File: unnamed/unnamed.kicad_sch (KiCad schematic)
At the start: 126 parts, among them J1 Serial, J2 Serial, J3 Conn_01x01_Female, J4 Conn_01x01_Female, J5 S3B-PH-SM4-TB(LF)(SN), J6 S3B-PH-SM4-TB(LF)(SN), J7 Conn_01x12_Female, J8 Conn_01x12_Female, SW1 SW_Push, SW10 SW_Push, SW11 SW_Push, SW12 SW_Push, SW13 SW_Push, SW14 SW_Push, SW15 SW_Push, SW16 SW_Push, SW17 SW_Push, SW18 SW_Push, SW19 SW_Push, SW2 SW_Push, SW20 SW_Push, SW21 SW_Push, SW22 SW_Push, SW23 SW_Push, SW24 SW_Push, SW25 SW_SPST, SW26 SW_SPST, SW27 SW_Push, SW28 SW_Push, SW29 SW_Push, SW3 SW_Push, SW30 SW_Push, SW31 SW_Push, SW32 SW_Push, SW33 SW_Push, SW34 SW_Push, SW35 SW_Push, SW36 SW_Push, SW4 SW_Push, SW5 SW_Push, SW6 SW_Push, SW7 SW_Push, SW8 SW_Push, SW9 SW_Push, U1 eliteC, U2 eliteC

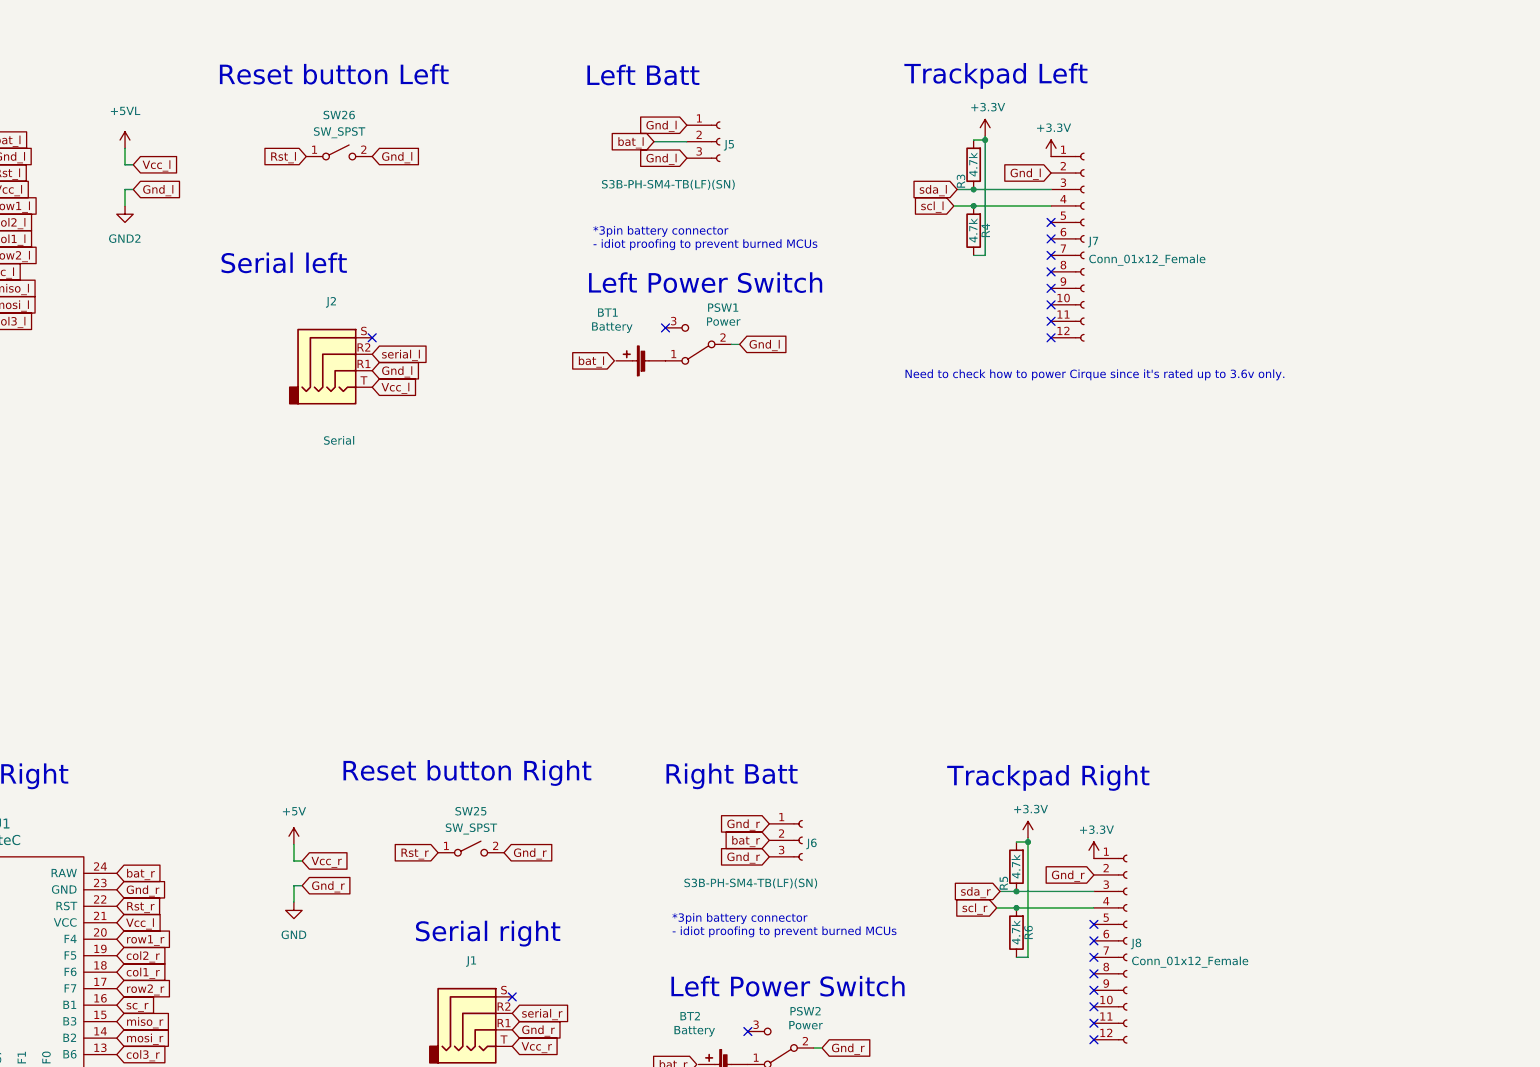
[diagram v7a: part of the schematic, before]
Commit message: Added OLED
SSD1306 OLED. Might include jumpers to bigger SH1107 (hi drashna!) OLED. Also planning to ad SPI screen pin headers.
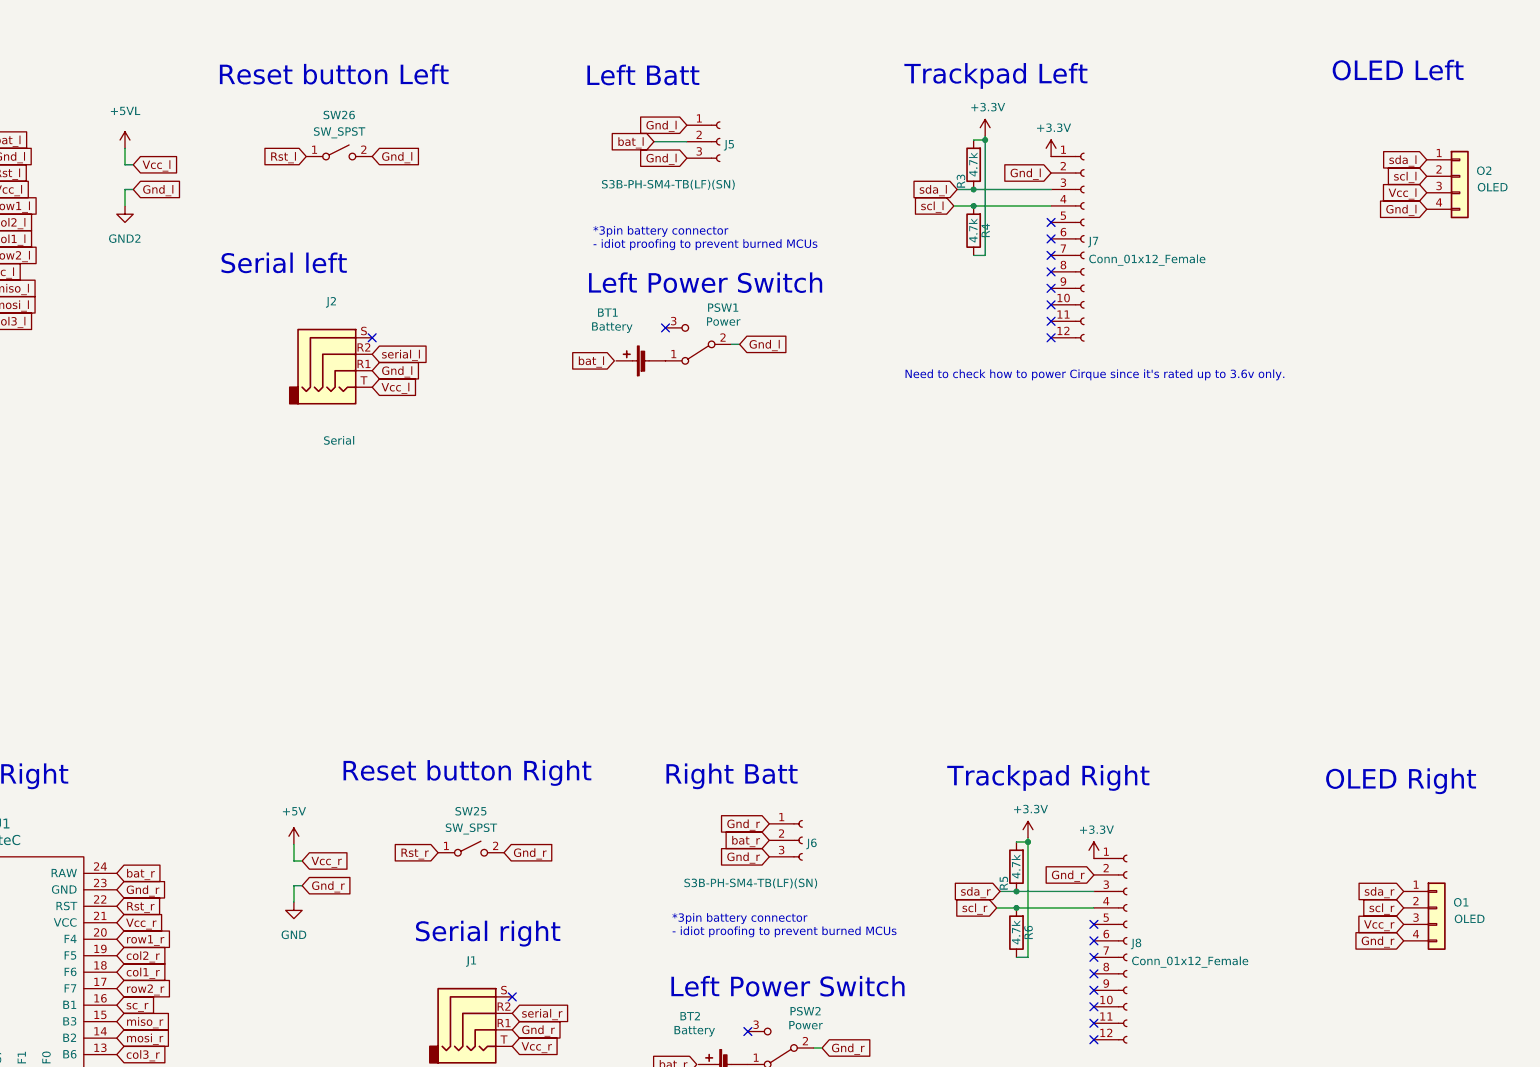
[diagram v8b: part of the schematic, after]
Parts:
- added O1, O2: OLED, swoop:OLED_jumpers, symbol Connector_Generic:Conn_01x04
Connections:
- net +5V: now also U1.21 (VCC), O1.3 (Pin_3)
- net +5VL: now also O2.3 (Pin_3); no longer U1.21 (VCC)
- net GND: now also O1.4 (Pin_4)
- net GND2: now also O2.4 (Pin_4)
- net scl_l: now also O2.2 (Pin_2)
- net scl_r: now also O1.2 (Pin_2)
- net sda_l: now also O2.1 (Pin_1)
- net sda_r: now also O1.1 (Pin_1)
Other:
- note added: "OLED Left"
- note added: "OLED Right"
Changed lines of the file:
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@@
     (effects (font (size 3 3)) (justify left bottom))
   )
+  (text "OLED Right" (at 525.272 136.144 0)
+    (effects (font (size 3 3)) (justify left bottom))
+  )
   (text "Reset button Right" (at 373.634 134.874 0)
     (effects (font (size 3 3)) (justify left bottom))
@@
     (effects (font (size 5 5)) (justify left bottom))
   )
+  (text "OLED Left" (at 526.288 26.924 0)
+    (effects (font (size 3 3)) (justify left bottom))
+  )
   (text "RGB - plate and thumb cluster" (at 73.3044 168.2242 180)
     (effects (font (size 1.27 1.27)) (justify right bottom))
@@
     )
   )
+  (global_label "sda_r" (shape input) (at 537.464 151.384 180)
+    (effects (font (size 1.27 1.27)) (justify right))
+    (property "Intersheet References" "${INTERSHEET_REFS}" (id 0) (at 508.254 96.774 0)
+      (effects (font (size 1.27 1.27)) hide)
+    )
+  )
   (global_label "Gnd_l" (shape input) (at 303.53 156.21 180)
     (effects (font (size 1.27 1.27)) (justify right))
@@
     )
   )
+  (global_label "scl_r" (shape input) (at 537.464 153.924 180)
+    (effects (font (size 1.27 1.27)) (justify right))
+    (property "Intersheet References" "${INTERSHEET_REFS}" (id 0) (at 508.254 99.314 0)
+      (effects (font (size 1.27 1.27)) hide)
+    )
+  )
   (global_label "Gnd_l" (shape input) (at 303.53 153.67 180)
     (effects (font (size 1.27 1.27)) (justify right))
@@
     )
   )
+  (global_label "Gnd_r" (shape input) (at 537.464 159.004 180)
+    (effects (font (size 1.27 1.27)) (justify right))
+    (property "Intersheet References" "${INTERSHEET_REFS}" (id 0) (at 660.654 228.854 0)
+      (effects (font (size 1.27 1.27)) hide)
+    )
+  )
   (global_label "col6_l" (shape input) (at 283.21 60.96 180)
     (effects (font (size 1.27 1.27)) (justify right))
@@
     )
   )
+  (global_label "Vcc_l" (shape input) (at 541.02 43.688 180)
+    (effects (font (size 1.27 1.27)) (justify right))
+    (property "Intersheet References" "${INTERSHEET_REFS}" (id 0) (at 664.21 113.538 0)
+      (effects (font (size 1.27 1.27)) hide)
+    )
+  )
   (global_label "row1_l" (shape input) (at 205.74 40.64 180)
     (effects (font (size 1.27 1.27)) (justify right))
@@
     )
   )
+  (global_label "Vcc_r" (shape input) (at 339.09 156.21 0)
+    (effects (font (size 1.27 1.27)) (justify left))
+    (property "Intersheet References" "${INTERSHEET_REFS}" (id 0) (at 215.9 86.36 0)
+      (effects (font (size 1.27 1.27)) hide)
+    )
+  )
   (global_label "row1_r" (shape input) (at 205.74 140.335 180)
     (effects (font (size 1.27 1.27)) (justify right))
@@
     )
   )
+  (global_label "sda_l" (shape input) (at 541.02 38.608 180)
+    (effects (font (size 1.27 1.27)) (justify right))
+    (property "Intersheet References" "${INTERSHEET_REFS}" (id 0) (at 511.81 -16.002 0)
+      (effects (font (size 1.27 1.27)) hide)
+    )
+  )
   (global_label "col3_r" (shape input) (at 339.09 176.53 0)
     (effects (font (size 1.27 1.27)) (justify left))
@@
     )
   )
+  (global_label "Vcc_r" (shape input) (at 537.464 156.464 180)
+    (effects (font (size 1.27 1.27)) (justify right))
+    (property "Intersheet References" "${INTERSHEET_REFS}" (id 0) (at 660.654 226.314 0)
+      (effects (font (size 1.27 1.27)) hide)
+    )
+  )
   (global_label "serial_l" (shape input) (at 378.46 68.58 0)
     (effects (font (size 1.27 1.27)) (justify left))
@@
     )
   )
-  (global_label "Vcc_l" (shape input) (at 339.09 156.21 0)
-    (effects (font (size 1.27 1.27)) (justify left))
-    (property "Intersheet References" "${INTERSHEET_REFS}" (id 0) (at 215.9 86.36 0)
-      (effects (font (size 1.27 1.27)) hide)
-    )
-  )
   (global_label "Gnd_l" (shape input) (at 283.21 43.18 180)
     (effects (font (size 1.27 1.27)) (justify right))
@@
     )
   )
+  (global_label "scl_l" (shape input) (at 541.02 41.148 180)
+    (effects (font (size 1.27 1.27)) (justify right))
+    (property "Intersheet References" "${INTERSHEET_REFS}" (id 0) (at 511.81 -13.462 0)
+      (effects (font (size 1.27 1.27)) hide)
+    )
+  )
   (global_label "col5_r" (shape input) (at 303.53 171.45 180)
     (effects (font (size 1.27 1.27)) (justify right))
@@
     )
   )
+  (global_label "Gnd_l" (shape input) (at 541.02 46.228 180)
+    (effects (font (size 1.27 1.27)) (justify right))
+    (property "Intersheet References" "${INTERSHEET_REFS}" (id 0) (at 664.21 116.078 0)
+      (effects (font (size 1.27 1.27)) hide)
+    )
+  )
   (global_label "bat_r" (shape input) (at 439.674 143.51 180)
     (effects (font (size 1.27 1.27)) (justify right))
@@
     (pin "T")
   )
+  (symbol (lib_id "Connector_Generic:Conn_01x04") (at 542.544 153.924 0) (unit 1)
+    (in_bom yes) (on_board yes)
+    (property "Reference" "O1" (id 0) (at 546.354 153.1135 0))
+    (property "Value" "OLED" (id 1) (at 547.624 155.6535 0))
+    (property "Footprint" "swoop:OLED_jumpers" (id 2) (at 542.544 153.924 0)
+      (effects (font (size 1.27 1.27)) hide)
+    )
+    (property "Datasheet" "" (id 3) (at 542.544 153.924 0)
+      (effects (font (size 1.27 1.27)) hide)
+    )
+    (pin "1")
+    (pin "2")
+    (pin "3")
+    (pin "4")
+  )
   (symbol (lib_id "Device:D") (at 71.12 48.26 180) (unit 1)
     (in_bom yes) (on_board yes)
@@
     (pin "2")
   )
+  (symbol (lib_id "Connector_Generic:Conn_01x04") (at 546.1 41.148 0) (unit 1)
+    (in_bom yes) (on_board yes)
+    (property "Reference" "O2" (id 0) (at 549.91 40.3375 0))
+    (property "Value" "OLED" (id 1) (at 551.18 42.8775 0))
+    (property "Footprint" "swoop:OLED_jumpers" (id 2) (at 546.1 41.148 0)
+      (effects (font (size 1.27 1.27)) hide)
+    )
+    (property "Datasheet" "" (id 3) (at 546.1 41.148 0)
+      (effects (font (size 1.27 1.27)) hide)
+    )
+    (pin "1")
+    (pin "2")
+    (pin "3")
+    (pin "4")
+  )
   (symbol (lib_id "Connector:Conn_01x12_Female") (at 488.188 50.8 0) (unit 1)
     (in_bom yes) (on_board yes) (fields_autoplaced)
@@
       (reference "J8") (unit 1) (value "Conn_01x12_Female") (footprint "prettylib:FPC-SMD_FH12-12S-0.5SH-55")
     )
+    (path "/8e810975-a4f5-47c2-90e3-7b00d8f30784"
+      (reference "O1") (unit 1) (value "OLED") (footprint "swoop:OLED_jumpers")
+    )
+    (path "/c51d5d6e-3b88-4f8e-8052-c5e71c69581c"
+      (reference "O2") (unit 1) (value "OLED") (footprint "swoop:OLED_jumpers")
+    )
     (path "/490427c5-7c38-4754-bcb1-0cc9dfe9dad4"
